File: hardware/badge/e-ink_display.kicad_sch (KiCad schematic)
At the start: 23 parts, among them J1201 MCU, Q1201 IRLML0100TRPBF, U1202 HC-FPC-05-09-24RLTAG

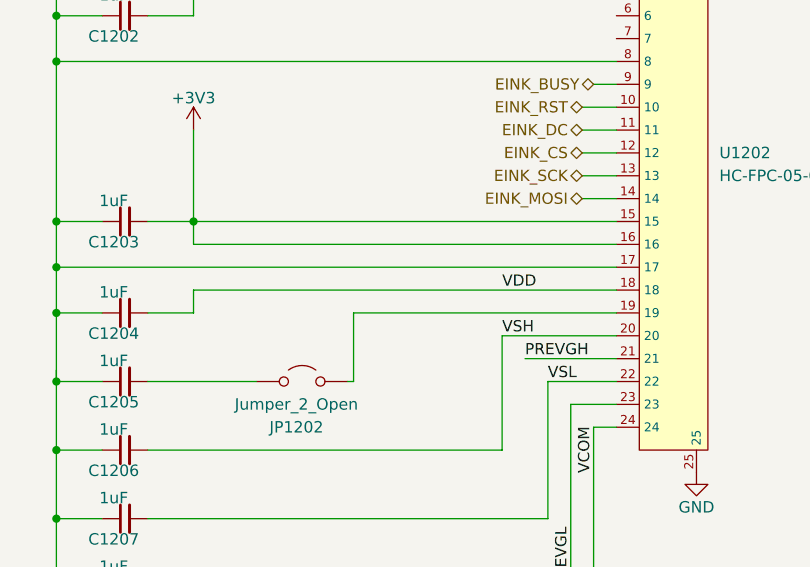
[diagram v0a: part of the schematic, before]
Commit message: feat: badge v2 PCB design with panelization support
Updated schematic and PCB layout for badge v2 revision. Added
panelization project with JLCPCB production files, panelize script,
and board SVG artwork.
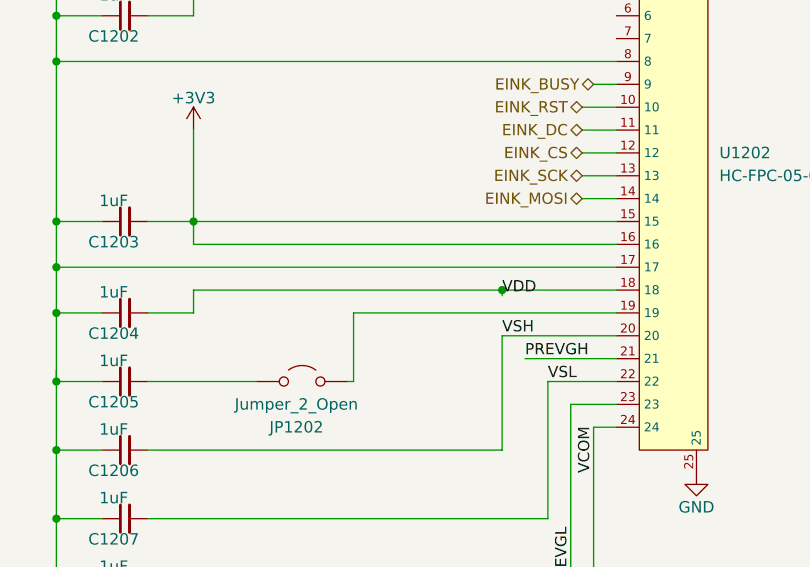
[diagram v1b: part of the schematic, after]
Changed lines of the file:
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@@
+	)
+	(junction
+		(at 78.105 83.185)
+		(diameter 0)
+		(color 0 0 0 0)
 	)
 	(junction
@@
 	(wire
 		(pts
-			(xy 43.815 83.185) (xy 90.805 83.185)
+			(xy 43.815 83.185) (xy 78.105 83.185)
 		)
 		(stroke
@@
 	(wire
 		(pts
+			(xy 78.105 83.82) (xy 78.105 83.185)
+		)
+		(stroke
+			(width 0.1524)
+			(type solid)
+		)
+	)
+	(wire
+		(pts
 			(xy 159.385 118.745) (xy 168.275 118.745)
 		)
@@
 			(width 0)
 			(type default)
+		)
+	)
+	(wire
+		(pts
+			(xy 78.105 83.185) (xy 90.805 83.185)
+		)
+		(stroke
+			(width 0.1524)
+			(type solid)
 		)
 	)
@@
 	)
 	(label "VDD"
-		(at 78.105 83.185 0)
+		(at 78.105 83.82 0)
 		(effects
 			(font
